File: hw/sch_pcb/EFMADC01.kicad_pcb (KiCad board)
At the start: 2 copper layers, 60.5 x 40.1 mm, 40 parts, among them J1 3.3-5V, J2 HEADER_2x01, J4 HEADER_2x01_PARALLEL, J5 HEADER_2x01_PARALLEL, J6 HEADER_2x01_PARALLEL, J7 HEADER_2x01_PARALLEL, J9 MCX, M1 RFShield_TwoPieces, M2 HOLE, M3 HOLE, M4 HOLE, M5 HOLE, U1 ISL21080DIH312Z-TK 1V25, U2 OPA314, U3 ISL21080CIH330Z-TK, U4 LTC1865-MS

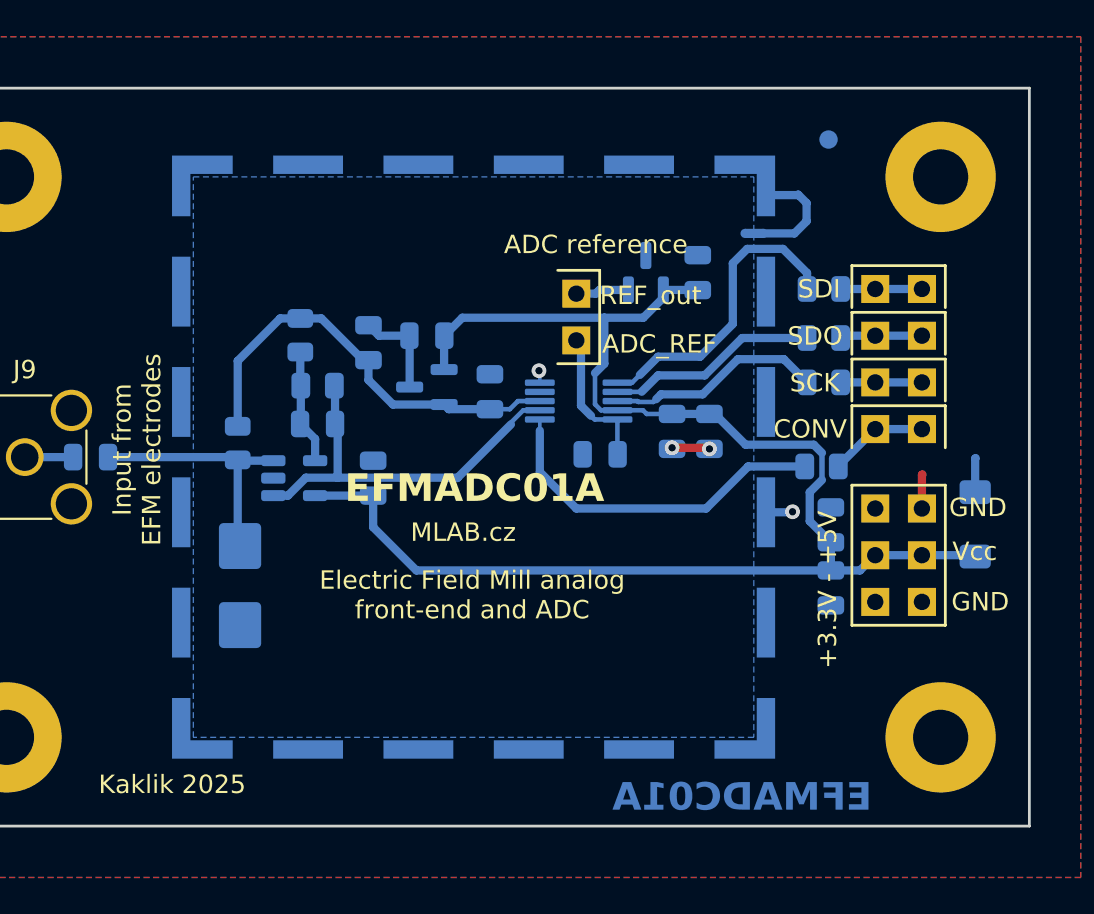
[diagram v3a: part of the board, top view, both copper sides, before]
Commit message: Improve layout, adding vias.
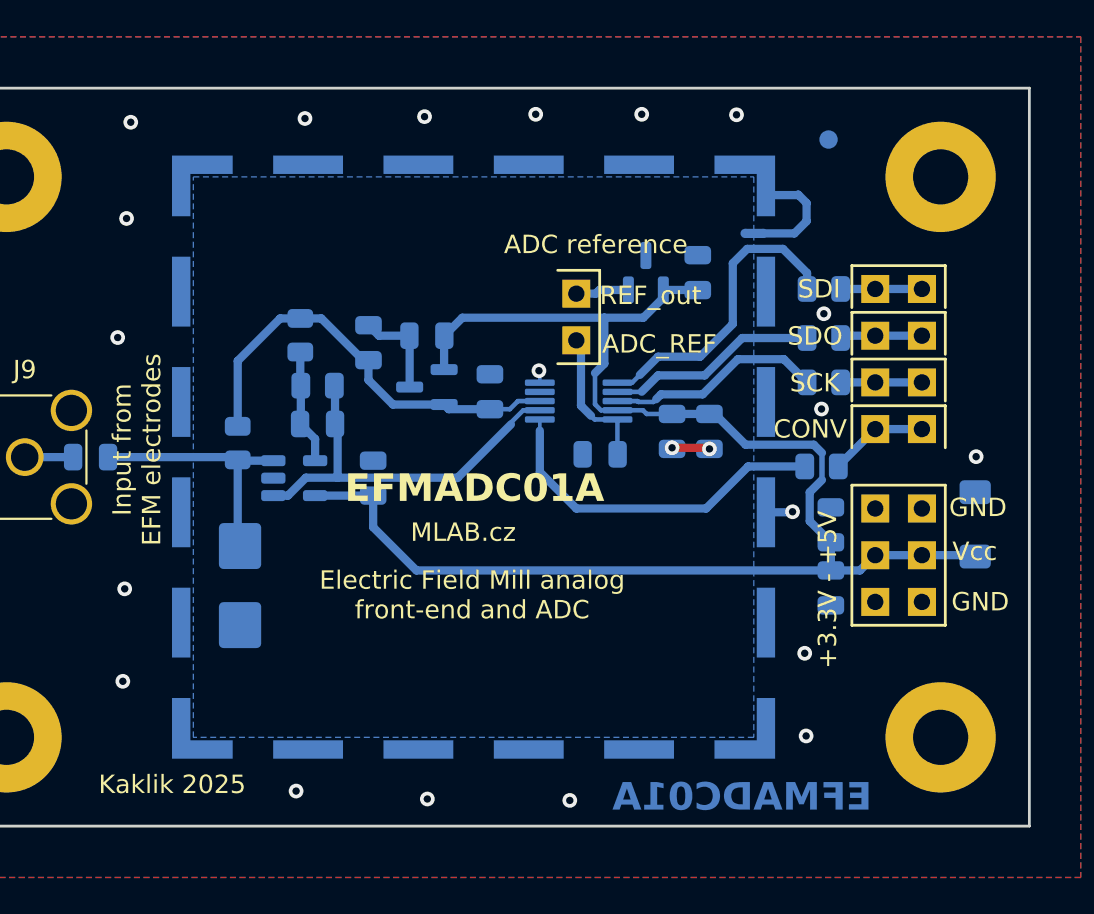
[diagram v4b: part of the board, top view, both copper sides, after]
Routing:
- net GND: track 14.4 -> 10.7 mm, vias 4 -> 22
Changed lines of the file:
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@@
 		(fp_line
 			(start 0.65 -1.56)
-			(end 0 -1.560001)
+			(end 0 -1.56)
 			(stroke
 				(width 0.12)
@@
 		(fp_line
 			(start -0.65 -1.56)
-			(end 0 -1.560001)
+			(end 0 -1.56)
 			(stroke
 				(width 0.12)
@@
 		(fp_line
 			(start 0.65 1.56)
-			(end 0 1.560001)
+			(end 0 1.56)
 			(stroke
 				(width 0.12)
@@
 		(fp_line
 			(start -0.65 1.56)
-			(end 0 1.560001)
+			(end 0 1.56)
 			(stroke
 				(width 0.12)
@@
 		(fp_poly
 			(pts
-				(xy -1.1625 1.51) (xy -1.4025 1.84) (xy -0.9225 1.839999) (xy -1.1625 1.51)
+				(xy -1.1625 1.51) (xy -1.4025 1.84) (xy -0.9225 1.84) (xy -1.1625 1.51)
 			)
 			(stroke
@@
 		)
 		(fp_line
-			(start 1.92 -1.700001)
-			(end -1.92 -1.700001)
+			(start 1.92 -1.7)
+			(end -1.92 -1.7)
 			(stroke
 				(width 0.05)
@@
 		)
 		(fp_line
-			(start -1.92 -1.700001)
-			(end -1.92 1.700001)
+			(start -1.92 -1.7)
+			(end -1.92 1.7)
 			(stroke
 				(width 0.05)
@@
 		)
 		(fp_line
-			(start 1.92 1.700001)
-			(end 1.92 -1.700001)
+			(start 1.92 1.7)
+			(end 1.92 -1.7)
 			(stroke
 				(width 0.05)
@@
 		)
 		(fp_line
-			(start -1.92 1.700001)
-			(end 1.92 1.700001)
+			(start -1.92 1.7)
+			(end 1.92 1.7)
 			(stroke
 				(width 0.05)
@@
 		)
 		(fp_line
-			(start -0.65 1.125001)
+			(start -0.65 1.125)
 			(end -0.65 -1.45)
 			(stroke
@@
 		(fp_line
 			(start -0.325 1.45)
-			(end -0.65 1.125001)
+			(end -0.65 1.125)
 			(stroke
 				(width 0.1)
@@
 		)
 		(pad "3" smd roundrect
-			(at 0.937501 0 90)
+			(at 0.9375 0 90)
 			(size 1.475 0.6)
 			(layers "B.Cu" "B.Paste" "B.Mask")
@@
 		(sheetname "Root")
 		(sheetfile "EFMADC01.kicad_sch")
-		(clearance 0.1)
 		(attr smd)
 		(fp_line
@@
 		(fp_poly
 			(pts
-				(xy -2.2125 1.435) (xy -2.4525 1.765) (xy -1.972501 1.765) (xy -2.2125 1.435)
+				(xy -2.2125 1.435) (xy -2.4525 1.765) (xy -1.9725 1.765) (xy -2.2125 1.435)
 			)
 			(stroke
@@
 		)
 		(fp_line
-			(start -3.18 -1.749999)
-			(end -3.18 1.749999)
+			(start -3.18 -1.75)
+			(end -3.18 1.75)
 			(stroke
 				(width 0.05)
@@
 		)
 		(fp_line
-			(start -3.18 1.749999)
-			(end 3.18 1.749999)
+			(start -3.18 1.75)
+			(end 3.18 1.75)
 			(stroke
 				(width 0.05)
@@
 		)
 		(fp_line
-			(start 3.18 -1.749999)
-			(end -3.18 -1.749999)
+			(start 3.18 -1.75)
+			(end -3.18 -1.75)
 			(stroke
 				(width 0.05)
@@
 		)
 		(fp_line
-			(start 3.18 1.749999)
-			(end 3.18 -1.749999)
+			(start 3.18 1.75)
+			(end 3.18 -1.75)
 			(stroke
 				(width 0.05)
@@
 		)
 		(pad "2" smd roundrect
-			(at -2.1125 0.499999)
+			(at -2.1125 0.5)
 			(size 1.625 0.35)
 			(layers "B.Cu" "B.Paste" "B.Mask")
@@
 		)
 		(pad "4" smd roundrect
-			(at -2.1125 -0.499999)
+			(at -2.1125 -0.5)
 			(size 1.625 0.35)
 			(layers "B.Cu" "B.Paste" "B.Mask")
@@
 		)
 		(pad "7" smd roundrect
-			(at 2.1125 -0.499999)
+			(at 2.1125 -0.5)
 			(size 1.625 0.35)
 			(layers "B.Cu" "B.Paste" "B.Mask")
@@
 		)
 		(pad "9" smd roundrect
-			(at 2.1125 0.499999)
+			(at 2.1125 0.5)
 			(size 1.625 0.35)
 			(layers "B.Cu" "B.Paste" "B.Mask")
@@
 		(tags "net tie")
 		(property "Reference" "JP1"
-			(at 0 1.2 0)
+			(at 0 1.2 180)
 			(layer "B.SilkS")
 			(hide yes)
@@
 		)
 		(property "Value" "Jumper_2_Bridged"
-			(at 0 -1.2 0)
+			(at 0 -1.2 180)
 			(layer "B.Fab")
 			(hide yes)
@@
 		(sheetfile "EFMADC01.kicad_sch")
 		(zone_connect 2)
-		(attr smd exclude_from_pos_files exclude_from_bom allow_missing_courtyard)
+		(attr exclude_from_pos_files exclude_from_bom allow_missing_courtyard)
 		(net_tie_pad_groups "1, 2")
 		(fp_poly
@@
 	)
 	(segment
-		(start 172.884 105.9652)
-		(end 172.9094 105.9398)
-		(width 0.45)
+		(start 160.626 104.619)
+		(end 160.311 104.619)
+		(width 0.2)
 		(layer "F.Cu")
 		(net 16)
 	)
-	(segment
-		(start 172.884 107.794)
-		(end 172.884 105.9652)
-		(width 0.45)
-		(layer "F.Cu")
+	(via
+		(at 166.5848 120.1638)
+		(size 0.8)
+		(drill 0.4)
+		(layers "F.Cu" "B.Cu")
 		(net 16)
 	)
-	(segment
-		(start 160.626 104.619)
-		(end 160.311 104.619)
-		(width 0.2)
-		(layer "F.Cu")
+	(via
+		(at 139.3306 86.585)
+		(size 0.8)
+		(drill 0.4)
+		(layers "F.Cu" "B.Cu")
+		(net 16)
+	)
+	(via
+		(at 145.833 86.4834)
+		(size 0.8)
+		(drill 0.4)
+		(layers "F.Cu" "B.Cu")
+		(net 16)
+	)
+	(via
+		(at 166.5086 115.668)
+		(size 0.8)
+		(drill 0.4)
+		(layers "F.Cu" "B.Cu")
+		(net 16)
+	)
+	(via
+		(at 129.4246 117.192)
+		(size 0.8)
+		(drill 0.4)
+		(layers "F.Cu" "B.Cu")
+		(net 16)
+	)
+	(via
+		(at 153.7324 123.669)
+		(size 0.8)
+		(drill 0.4)
+		(layers "F.Cu" "B.Cu")
+		(net 16)
+	)
+	(via
+		(at 129.1452 98.4976)
+		(size 0.8)
+		(drill 0.4)
+		(layers "F.Cu" "B.Cu")
+		(net 16)
+	)
+	(via
+		(at 175.8304 104.9746)
+		(size 0.8)
+		(drill 0.4)
+		(layers "F.Cu" "B.Cu")
 		(net 16)
 	)
@@
 	)
 	(via
+		(at 157.644 86.3564)
+		(size 0.8)
+		(drill 0.4)
+		(layers "F.Cu" "B.Cu")
+		(net 16)
+	)
+	(via
+		(at 167.423 102.3838)
+		(size 0.8)
+		(drill 0.4)
+		(layers "F.Cu" "B.Cu")
+		(net 16)
+	)
+	(via
 		(at 152.056 100.301)
 		(size 0.8)
@@
 	)
 	(via
+		(at 138.848 123.161)
+		(size 0.8)
+		(drill 0.4)
+		(layers "F.Cu" "B.Cu")
+		(net 16)
+	)
+	(via
 		(at 159.295 104.492)
 		(size 0.8)
@@
 	)
 	(via
+		(at 151.8782 86.3564)
+		(size 0.8)
+		(drill 0.4)
+		(layers "F.Cu" "B.Cu")
+		(net 16)
+	)
+	(via
 		(at 161.327 104.553)
 		(size 0.8)
@@
 		(net 16)
 	)
-	(segment
-		(start 175.7796 105.0762)
-		(end 175.805 105.0508)
-		(width 0.45)
-		(layer "B.Cu")
+	(via
+		(at 145.9854 123.5928)
+		(size 0.8)
+		(drill 0.4)
+		(layers "F.Cu" "B.Cu")
+		(net 16)
+	)
+	(via
+		(at 129.6278 92.0206)
+		(size 0.8)
+		(drill 0.4)
+		(layers "F.Cu" "B.Cu")
+		(net 16)
+	)
+	(via
+		(at 129.8564 86.7882)
+		(size 0.8)
+		(drill 0.4)
+		(layers "F.Cu" "B.Cu")
+		(net 16)
+	)
+	(via
+		(at 129.5262 112.1628)
+		(size 0.8)
+		(drill 0.4)
+		(layers "F.Cu" "B.Cu")
+		(net 16)
+	)
+	(via
+		(at 162.8002 86.3818)
+		(size 0.8)
+		(drill 0.4)
+		(layers "F.Cu" "B.Cu")
+		(net 16)
+	)
+	(via
+		(at 167.55 97.2022)
+		(size 0.8)
+		(drill 0.4)
+		(layers "F.Cu" "B.Cu")
 		(net 16)
 	)
@@
 		(width 0.45)
 		(layer "B.Cu")
-		(net 16)
-	)
-	(segment
-		(start 175.7796 106.9076)
-		(end 175.7796 105.0762)
-		(width 0.45)
-		(layer "B.Cu")

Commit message: Cleanup net names in schematics.
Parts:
- U1: value ISL21080DIH312Z-TK 1V25 -> ISL21080CIH315ZT
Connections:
- net /REF_1V25 renamed /REF
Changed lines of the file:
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@@
 	(net 1 "GNDA")
 	(net 2 "Net-(D1-A1)")
-	(net 3 "/REF_1V25")
+	(net 3 "/REF")
 	(net 4 "Net-(J9-In)")
 	(net 5 "Net-(U2--)")
@@
 			)
 		)
-		(property "UST_ID" ""
+		(property "UST_ID" "67d36d64ee7fc534862c3ebc"
 			(at 0 0 -90)
 			(unlocked yes)
@@
 			(layers "B.Cu" "B.Paste" "B.Mask")
 			(roundrect_rratio 0.25)
-			(net 3 "/REF_1V25")
+			(net 3 "/REF")
 			(pintype "passive")
 		)
@@
 			(layers "B.Cu" "B.Paste" "B.Mask")
 			(roundrect_rratio 0.243902)
-			(net 3 "/REF_1V25")
+			(net 3 "/REF")
 			(pintype "passive")
 		)
@@
 			)
 		)
+		(property "UST_ID" "651eae84462c6d9e7205573b"
+			(at 0 0 0)
+			(unlocked yes)
+			(layer "B.Fab")
+			(hide yes)
+			(effects
+				(font
+					(size 1 1)
+					(thickness 0.15)
+				)
+				(justify mirror)
+			)
+		)
 		(property ki_fp_filters "MSOP*3x3mm*P0.5mm*")
 		(sheetname "Root")
@@
 			(layers "B.Cu" "B.Paste" "B.Mask")
 			(roundrect_rratio 0.25)
-			(net 3 "/REF_1V25")
+			(net 3 "/REF")
 			(pinfunction "CH1")
 			(pintype "input")
@@
 			(layers "B.Cu" "B.Paste" "B.Mask")
 			(roundrect_rratio 0.243902)
-			(net 3 "/REF_1V25")
+			(net 3 "/REF")
 			(pintype "passive")
 		)
@@
 			(layers "B.Cu" "B.Paste" "B.Mask")
 			(roundrect_rratio 0.25)
-			(net 3 "/REF_1V25")
+			(net 3 "/REF")
 			(pintype "passive")
 		)
@@
 			)
 		)
-		(property "Value" "ISL21080DIH312Z-TK  1V25"
+		(property "Value" "ISL21080CIH315ZT"
 			(at 0 -2.4 0)
 			(layer "B.Fab")
@@
 			)
 		)
-		(property "Description" "2.0V 25μA Micropower Voltage Reference, SOT-23"
+		(property "Description" "1.5V 25μA Micropower Voltage Reference, SOT-23"
 			(at 0 0 0)
 			(layer "B.Fab")
@@
 			)
 		)
-		(property "UST_ID" "5c70984712875079b91f8b7a"
+		(property "UST_ID" "5c70984712875079b91f8b0a"
 			(at 0 0 0)
 			(unlocked yes)
@@
 			(layers "B.Cu" "B.Paste" "B.Mask")
 			(roundrect_rratio 0.25)
-			(net 3 "/REF_1V25")
+			(net 3 "/REF")
 			(pinfunction "Vout")
 			(pintype "power_out")

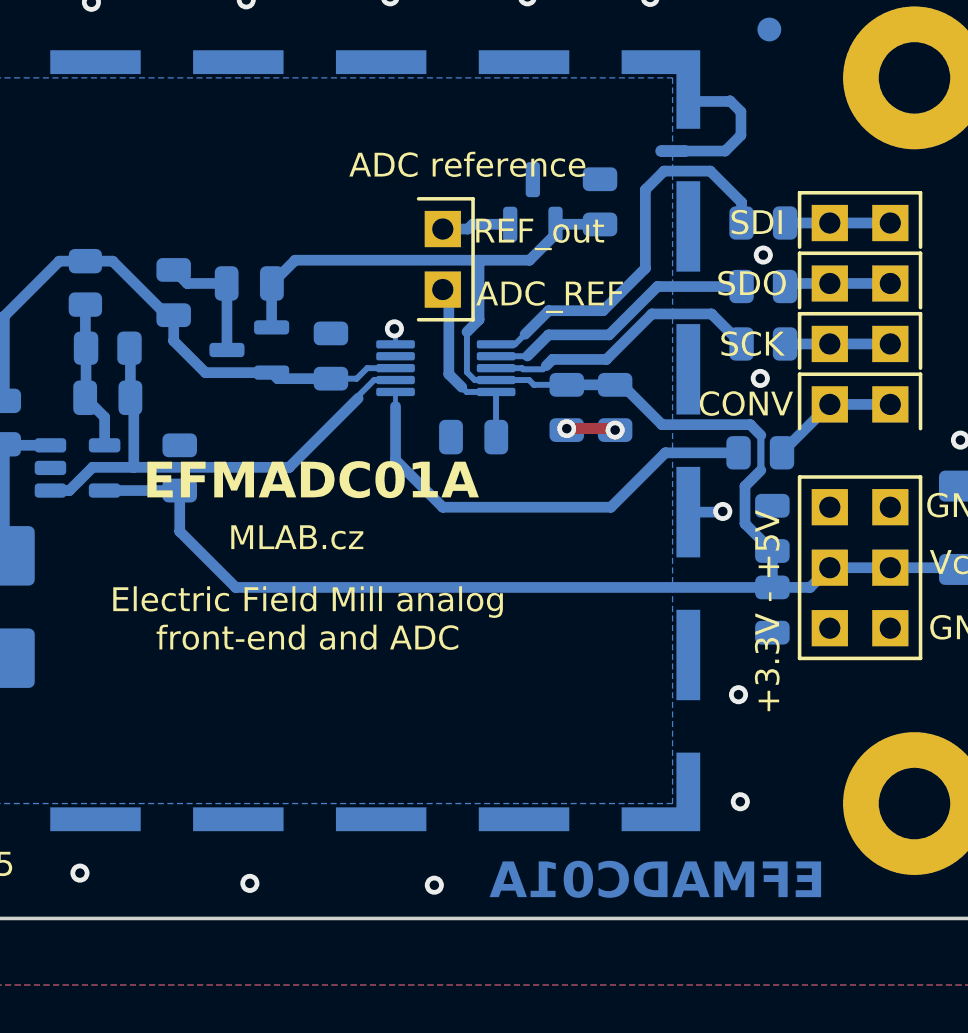
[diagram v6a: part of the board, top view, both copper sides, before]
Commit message: Implement buffer to reference voltage.
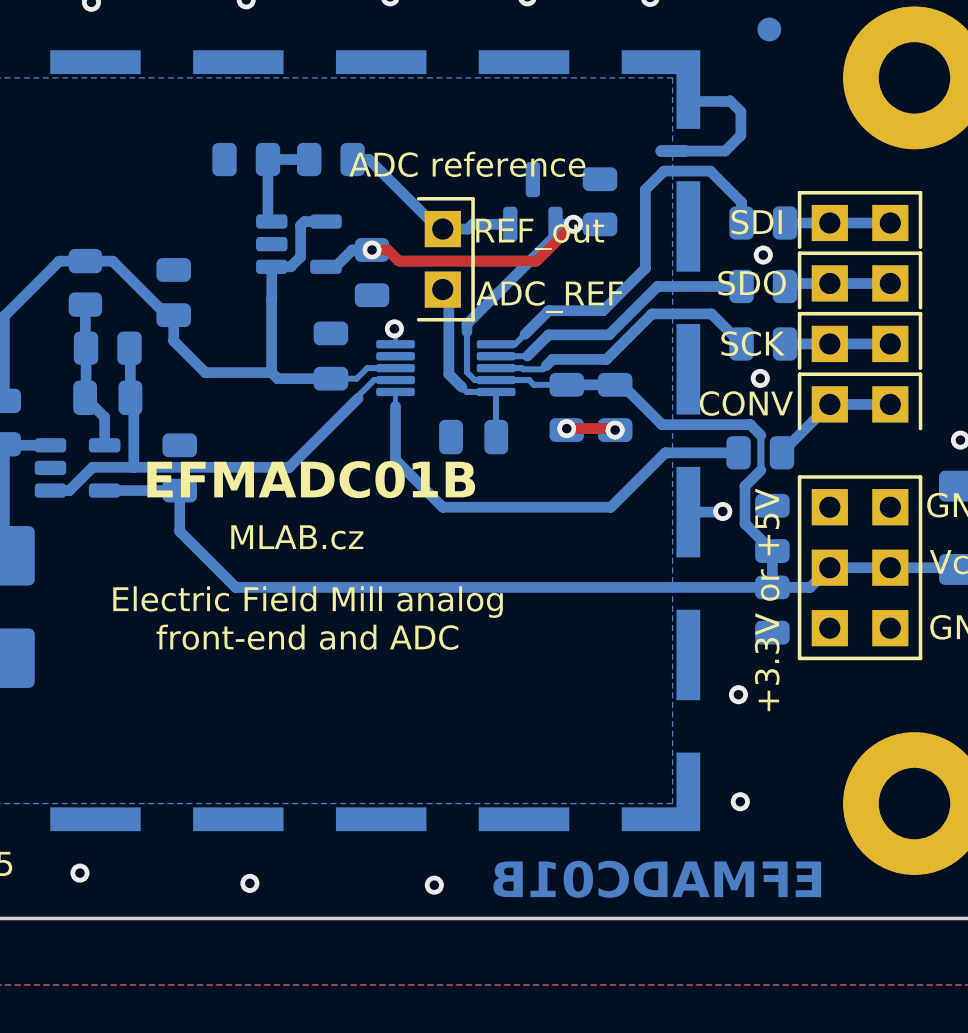
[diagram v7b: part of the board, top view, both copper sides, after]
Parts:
- removed C7: 100nF, Capacitor_SMD:C_0805_2012Metric
- removed U1: ISL21080CIH315ZT, Package_TO_SOT_SMD:SOT-23
- added C13: 100nF, Capacitor_SMD:C_0805_2012Metric, B.Cu at (151.1, 97.9)
- added R8: 1k, Resistor_SMD:R_0805_2012Metric, B.Cu at (145.8, 93.2)
- added R9: 1k, Resistor_SMD:R_0805_2012Metric, B.Cu at (149.4, 93.2)
- added U5: OPA314, Package_TO_SOT_SMD:SOT-23-5, B.Cu at (148.0, 96.7)
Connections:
- net Net-(U3-Vout) renamed /ADC_REF
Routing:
- net /REF: track 23.8 -> 32.1 mm
- net GNDA: track 5.26 -> 0.00 mm
- net /ADC_REF: track 2.92 -> 7.91 mm
- net Net-(U5-+): track 0.00 -> 4.40 mm
- net VCC: track 81.6 -> 83.2 mm, vias 0 -> 2
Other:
- board text added: "+3.3V or +5V"
- board text added: "EFMADC01B"
- board text removed: "+3.3V - +5V"
- board text removed: "EFMADC01A"
